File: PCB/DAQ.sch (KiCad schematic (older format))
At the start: 45 parts, among them IC1 MAX743CWE+, J1 Arduino_Mega_Header, J10 Conn_01x01, J11 Conn_01x01, J12 Conn_01x01, J2 Conn_01x07, J3 Conn_01x08, J4 Conn_01x08, J5 Conn_02x18_Counter_Clockwise, J6 Conn_01x10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

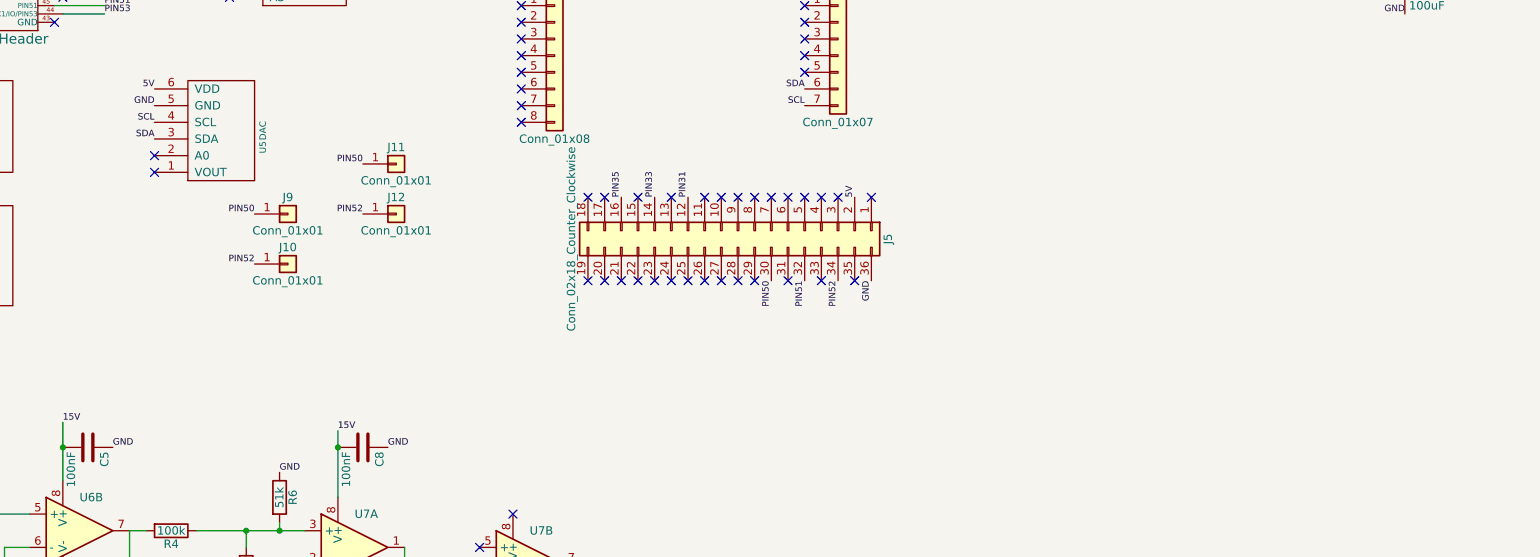
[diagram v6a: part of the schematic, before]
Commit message: Added analog part of DAC to PCB
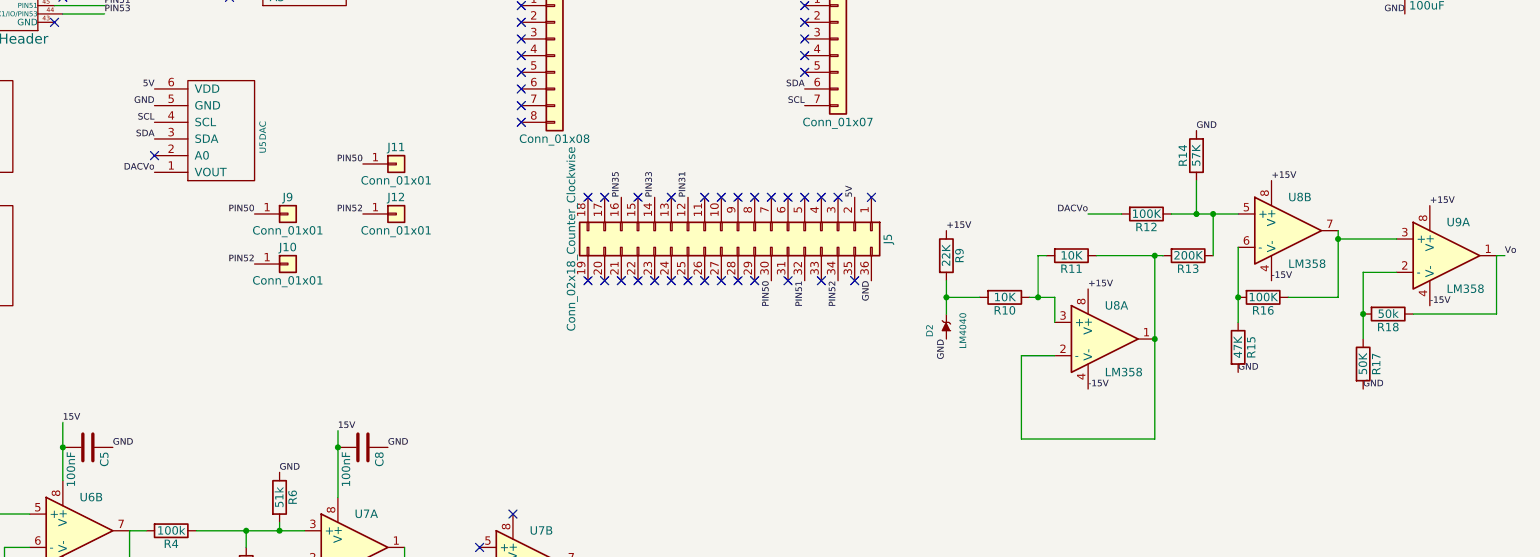
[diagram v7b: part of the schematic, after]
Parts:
- added D2: LM4040, TH-R:R-C-L-D, symbol LM4040
- added R10, R11: 10K, Resistors_THT:R_Axial_DIN0207_L6.3mm_D2.5mm_P7.62mm_Horizontal, symbol R
- added R12, R16: 100K, Resistors_THT:R_Axial_DIN0207_L6.3mm_D2.5mm_P7.62mm_Horizontal, symbol R
- added R13: 200K, Resistors_THT:R_Axial_DIN0207_L6.3mm_D2.5mm_P7.62mm_Horizontal, symbol R
- added R14: 57K, Resistors_THT:R_Axial_DIN0207_L6.3mm_D2.5mm_P7.62mm_Horizontal, symbol R
- added R15: 47K, Resistors_THT:R_Axial_DIN0207_L6.3mm_D2.5mm_P7.62mm_Horizontal, symbol R
- added R17: 50K, Resistors_THT:R_Axial_DIN0207_L6.3mm_D2.5mm_P7.62mm_Horizontal, symbol R
- added R18: 50k, Resistors_THT:R_Axial_DIN0207_L6.3mm_D2.5mm_P7.62mm_Horizontal, symbol R
- added R9: 22K, Resistors_THT:R_Axial_DIN0207_L6.3mm_D2.5mm_P7.62mm_Horizontal, symbol R
- added U8, U9: LM358, Housings_DIP:DIP-8_W7.62mm, symbol LM358
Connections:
- net +15V: now also R9.1, U8.8 (V+), U8.8 (V+), U9.8 (V+)
- net -15V: now also U8.4 (V-), U8.4 (V-), U9.4 (V-)
- net GND: now also D2.2 (A), R14.2, R15.2, R17.2
- net DACVo: now reaches U5.1 (VOUT)
- net DACVo: now also R12.2
- new net: R11.1, R13.2, U8.1, U8.2 (-)
- new net: R10.1, R11.2, U8.3 (+)
- new net: R17.1, R18.2, U9.2 (-)
- new net: R16.1, U8.7, U9.3 (+)
- new net: R12.1, R13.1, R14.1, U8.5 (+)
- new net: R15.1, R16.2, U8.6 (-)
- new net: D2.1 (K), R10.2, R9.2
- new net Vo: R18.1, U9.1
- no-connect marks 138 -> 137
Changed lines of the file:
@@
 NoConn ~ 3450 3500
 NoConn ~ 3000 4550
-NoConn ~ 3000 4650
 $Comp
 L Conn_01x07 J2
@@
 Text Label 3600 5200 2    39   ~ 0
 PIN52
+$Comp
+L LM358 U8
+U 1 1 5ACCFE80
+P 8700 5650
+F 0 "U8" H 8700 5850 50  0000 L CNN
+F 1 "LM358" H 8700 5450 50  0000 L CNN
+F 2 "Housings_DIP:DIP-8_W7.62mm" H 8700 5650 50  0001 C CNN
+F 3 "" H 8700 5650 50  0001 C CNN
+	1    8700 5650
+	1    0    0    -1
+$EndComp
+$Comp
+L LM358 U9
+U 1 1 5ACCFF07
+P 10750 5150
+F 0 "U9" H 10750 5350 50  0000 L CNN
+F 1 "LM358" H 10750 4950 50  0000 L CNN
+F 2 "Housings_DIP:DIP-8_W7.62mm" H 10750 5150 50  0001 C CNN
+F 3 "" H 10750 5150 50  0001 C CNN
+	1    10750 5150
+	1    0    0    -1
+$EndComp
+$Comp
+L LM358 U8
+U 2 1 5ACD0129
+P 9800 5000
+F 0 "U8" H 9800 5200 50  0000 L CNN
+F 1 "LM358" H 9800 4800 50  0000 L CNN
+F 2 "Housings_DIP:DIP-8_W7.62mm" H 9800 5000 50  0001 C CNN
+F 3 "" H 9800 5000 50  0001 C CNN
+	2    9800 5000
+	1    0    0    -1
+$EndComp
+$Comp
+L LM4040 D2
+U 1 1 5ACD0290
+P 7750 5600
+F 0 "D2" H 7750 5700 40  0000 C CNN
+F 1 "LM4040" H 7750 5500 40  0000 C CNN
+F 2 "TH-R:R-C-L-D" H 7750 5600 60  0001 C CNN
+F 3 "" H 7750 5600 60  0000 C CNN
+	1    7750 5600
+	0    -1   -1   0
+$EndComp
+$Comp
+L R R9
+U 1 1 5ACD033B
+P 7750 5150
+F 0 "R9" V 7830 5150 50  0000 C CNN
+F 1 "22K" V 7750 5150 50  0000 C CNN
+F 2 "Resistors_THT:R_Axial_DIN0207_L6.3mm_D2.5mm_P7.62mm_Horizontal" V 7680 5150 50  0001 C CNN
+F 3 "" H 7750 5150 50  0001 C CNN
+	1    7750 5150
+	1    0    0    -1
+$EndComp
+$Comp
+L R R10
+U 1 1 5ACD03DC
+P 8100 5400
+F 0 "R10" V 8180 5400 50  0000 C CNN
+F 1 "10K" V 8100 5400 50  0000 C CNN
+F 2 "Resistors_THT:R_Axial_DIN0207_L6.3mm_D2.5mm_P7.62mm_Horizontal" V 8030 5400 50  0001 C CNN
+F 3 "" H 8100 5400 50  0001 C CNN
+	1    8100 5400
+	0    1    1    0
+$EndComp
+$Comp
+L R R11
+U 1 1 5ACD04A7
+P 8500 5150
+F 0 "R11" V 8580 5150 50  0000 C CNN
+F 1 "10K" V 8500 5150 50  0000 C CNN
+F 2 "Resistors_THT:R_Axial_DIN0207_L6.3mm_D2.5mm_P7.62mm_Horizontal" V 8430 5150 50  0001 C CNN
+F 3 "" H 8500 5150 50  0001 C CNN
+	1    8500 5150
+	0    1    1    0
+$EndComp
+$Comp
+L R R12
+U 1 1 5ACD075C
+P 8950 4900
+F 0 "R12" V 9030 4900 50  0000 C CNN
+F 1 "100K" V 8950 4900 50  0000 C CNN
+F 2 "Resistors_THT:R_Axial_DIN0207_L6.3mm_D2.5mm_P7.62mm_Horizontal" V 8880 4900 50  0001 C CNN
+F 3 "" H 8950 4900 50  0001 C CNN
+	1    8950 4900
+	0    1    1    0
+$EndComp
+$Comp
+L R R14
+U 1 1 5ACD08D8
+P 9250 4550
+F 0 "R14" V 9330 4550 50  0000 C CNN
+F 1 "57K" V 9250 4550 50  0000 C CNN
+F 2 "Resistors_THT:R_Axial_DIN0207_L6.3mm_D2.5mm_P7.62mm_Horizontal" V 9180 4550 50  0001 C CNN
+F 3 "" H 9250 4550 50  0001 C CNN
+	1    9250 4550
+	-1   0    0    1
+$EndComp
+$Comp
+L R R15
+U 1 1 5ACD0977
+P 9500 5700
+F 0 "R15" V 9580 5700 50  0000 C CNN
+F 1 "47K" V 9500 5700 50  0000 C CNN
+F 2 "Resistors_THT:R_Axial_DIN0207_L6.3mm_D2.5mm_P7.62mm_Horizontal" V 9430 5700 50  0001 C CNN
+F 3 "" H 9500 5700 50  0001 C CNN
+	1    9500 5700
+	1    0    0    -1
+$EndComp
+$Comp
+L R R16
+U 1 1 5ACD0A0E
+P 9650 5400
+F 0 "R16" V 9730 5400 50  0000 C CNN
+F 1 "100K" V 9650 5400 50  0000 C CNN
+F 2 "Resistors_THT:R_Axial_DIN0207_L6.3mm_D2.5mm_P7.62mm_Horizontal" V 9580 5400 50  0001 C CNN
+F 3 "" H 9650 5400 50  0001 C CNN
+	1    9650 5400
+	0    1    1    0
+$EndComp
+$Comp
+L R R17
+U 1 1 5ACD0D00
+P 10250 5800
+F 0 "R17" V 10330 5800 50  0000 C CNN
+F 1 "50K" V 10250 5800 50  0000 C CNN
+F 2 "Resistors_THT:R_Axial_DIN0207_L6.3mm_D2.5mm_P7.62mm_Horizontal" V 10180 5800 50  0001 C CNN
+F 3 "" H 10250 5800 50  0001 C CNN
+	1    10250 5800
+	1    0    0    -1
+$EndComp
+$Comp
+L R R18
+U 1 1 5ACD0D06
+P 10400 5500
+F 0 "R18" V 10480 5500 50  0000 C CNN
+F 1 "50k" V 10400 5500 50  0000 C CNN
+F 2 "Resistors_THT:R_Axial_DIN0207_L6.3mm_D2.5mm_P7.62mm_Horizontal" V 10330 5500 50  0001 C CNN
+F 3 "" H 10400 5500 50  0001 C CNN
+	1    10400 5500
+	0    1    1    0
+$EndComp
+Text Label 7750 5650 3    39   ~ 0
+GND
+Wire Wire Line
+	7750 5500 7750 5300
+Wire Wire Line
+	7950 5400 7750 5400
+Connection ~ 7750 5400
+Text Label 7750 5000 0    39   ~ 0
++15V
+Wire Wire Line
+	8250 5400 8400 5400
+Wire Wire Line
+	8400 5400 8400 5550
+Wire Wire Line
+	8400 5750 8200 5750
+Wire Wire Line
+	8200 5750 8200 6250
+Wire Wire Line
+	8200 6250 9000 6250
+Wire Wire Line
+	9000 6250 9000 5150
+Wire Wire Line
+	8300 5400 8300 5150
+Wire Wire Line
+	8300 5150 8350 5150
+Connection ~ 8300 5400
+Wire Wire Line
+	8650 5150 9050 5150
+Connection ~ 9000 5650
+$Comp
+L R R13
+U 1 1 5ACD2C7F
+P 9200 5150
+F 0 "R13" V 9280 5150 50  0000 C CNN
+F 1 "200K" V 9200 5150 50  0000 C CNN
+F 2 "Resistors_THT:R_Axial_DIN0207_L6.3mm_D2.5mm_P7.62mm_Horizontal" V 9130 5150 50  0001 C CNN
+F 3 "" H 9200 5150 50  0001 C CNN
+	1    9200 5150
+	0    1    1    0
+$EndComp
+Connection ~ 9000 5150
+Wire Wire Line
+	9350 5150 9350 4900
+Wire Wire Line
+	9100 4900 9500 4900
+Connection ~ 9350 4900
+Wire Wire Line
+	9250 4700 9250 4900
+Connection ~ 9250 4900
+Wire Wire Line
+	8800 4900 8600 4900
+Text Label 9250 4400 0    39   ~ 0
+GND
+Text Label 8600 5350 0    39   ~ 0
++15V
+Text Label 8600 5950 0    39   ~ 0
+-15V
+Text Label 9700 4700 0    39   ~ 0
++15V
+Text Label 9700 5300 0    39   ~ 0
+-15V
+Text Label 10650 4850 0    39   ~ 0
++15V
+Text Label 10650 5450 0    39   ~ 0
+-15V
+Text Label 8600 4900 2    39   ~ 0
+DACVo
+Text Label 3000 4650 2    39   ~ 0
+DACVo
+Wire Wire Line
+	9500 5100 9500 5550
+Wire Wire Line
+	9800 5400 10100 5400
+Wire Wire Line
+	10100 5400 10100 5000
+Connection ~ 9500 5400
+Text Label 9500 5850 0    39   ~ 0
+GND
+Wire Wire Line
+	10450 5050 10100 5050
+Connection ~ 10100 5050
+Wire Wire Line
+	10450 5250 10250 5250
+Wire Wire Line
+	10250 5250 10250 5650
+Connection ~ 10250 5500
+Wire Wire Line
+	10550 5500 11050 5500
+Wire Wire Line
+	11050 5500 11050 5150
+Wire Wire Line
+	11050 5150 11100 5150
+Text Label 10250 5950 0    39   ~ 0
+GND
+Text Label 11100 5150 0    39   ~ 0
+Vo
 $EndSCHEMATC

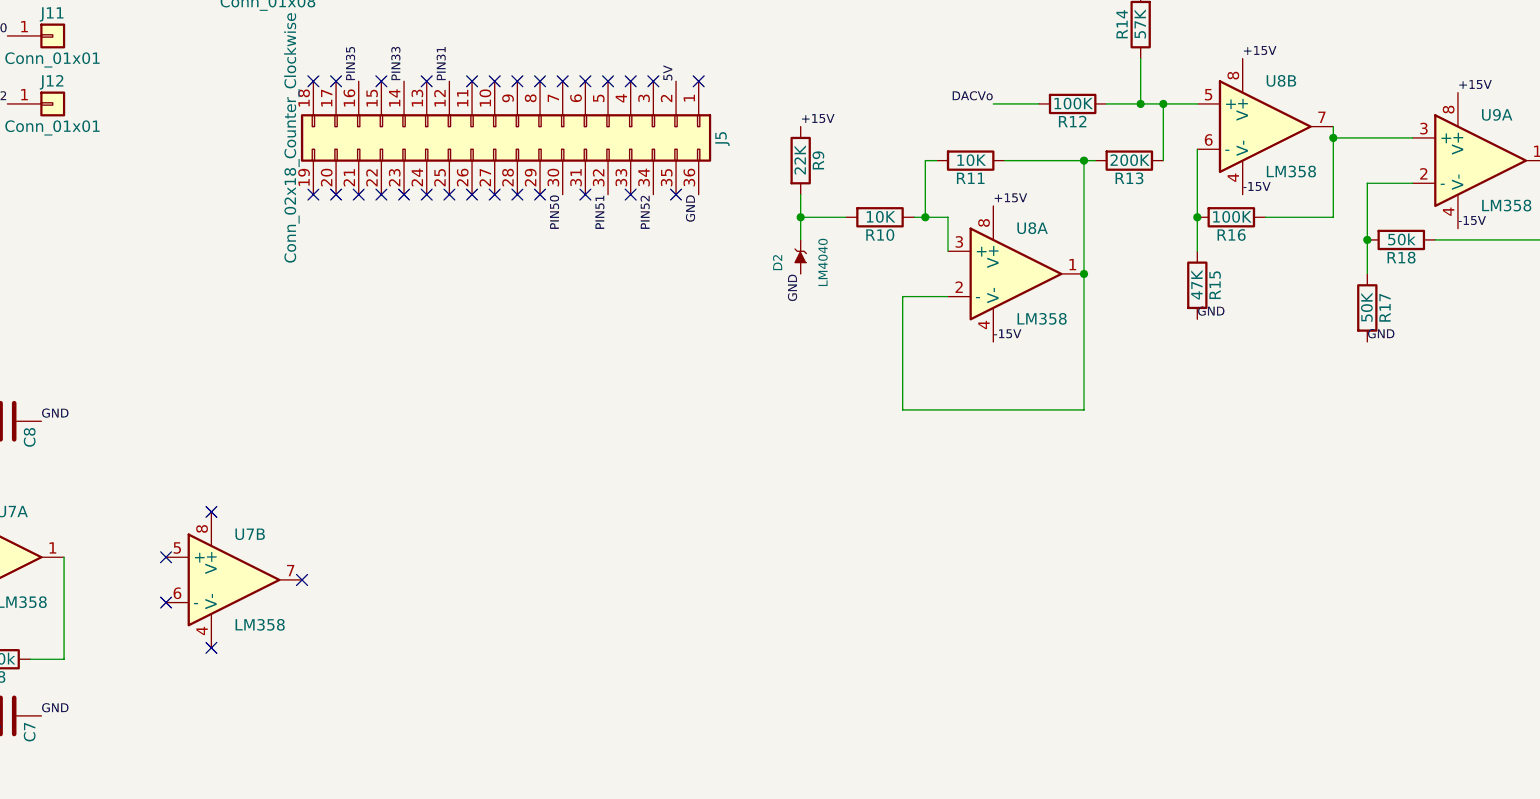
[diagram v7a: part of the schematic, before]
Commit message: Analog parts of the PCB upgraded
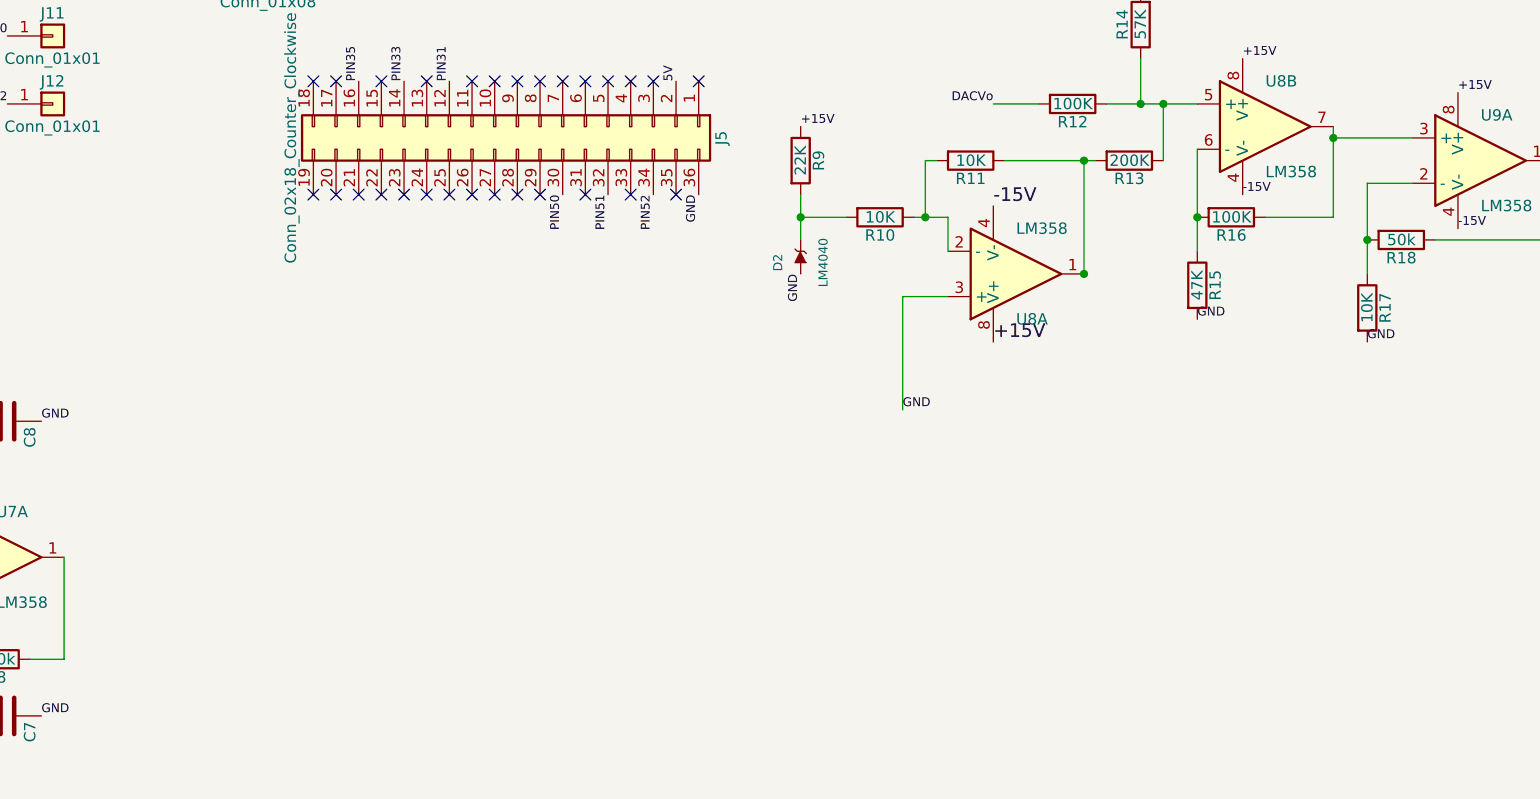
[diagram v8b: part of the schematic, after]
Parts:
- removed unit 2 of U7
- R17: value 50K -> 10K
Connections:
- net GND: now also U8.3 (+)
- net at R11.1, R13.2, U8.1: no longer U8.2 (-)
- net at R10.1, R11.2: now also U8.2 (-); no longer U8.3 (+)
- no-connect marks 137 -> 132
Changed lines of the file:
@@
 	0    1    1    0
 $EndComp
-$Comp
-L LM358 U7
-U 2 1 5AAC3CAA
-P 5250 7000
-F 0 "U7" H 5250 7200 50  0000 L CNN
-F 1 "LM358" H 5250 6800 50  0000 L CNN
-F 2 "Housings_DIP:DIP-8_W7.62mm" H 5250 7000 50  0001 C CNN
-F 3 "" H 5250 7000 50  0001 C CNN
-	2    5250 7000
-	1    0    0    -1
-$EndComp
-NoConn ~ 4950 6900
-NoConn ~ 4950 7100
-NoConn ~ 5150 7300
-NoConn ~ 5150 6700
-NoConn ~ 5550 7000
 Text Label 2450 6150 0    39   ~ 0
 15V
@@
 F 3 "" H 8700 5650 50  0001 C CNN
 	1    8700 5650
-	1    0    0    -1
+	1    0    0    1
 $EndComp
 $Comp
@@
 P 10250 5800
 F 0 "R17" V 10330 5800 50  0000 C CNN
-F 1 "50K" V 10250 5800 50  0000 C CNN
+F 1 "10K" V 10250 5800 50  0000 C CNN
 F 2 "Resistors_THT:R_Axial_DIN0207_L6.3mm_D2.5mm_P7.62mm_Horizontal" V 10180 5800 50  0001 C CNN
 F 3 "" H 10250 5800 50  0001 C CNN
@@
 	8200 5750 8200 6250
 Wire Wire Line
-	8200 6250 9000 6250
-Wire Wire Line
-	9000 6250 9000 5150
-Wire Wire Line
 	8300 5400 8300 5150
 Wire Wire Line
@@
 Text Label 9250 4400 0    39   ~ 0
 GND
-Text Label 8600 5350 0    39   ~ 0
-+15V
-Text Label 8600 5950 0    39   ~ 0
--15V
 Text Label 9700 4700 0    39   ~ 0
 +15V
@@
 Text Label 11100 5150 0    39   ~ 0
 Vo
+Text Label 8600 5350 0    60   ~ 0
+-15V
+Text Label 8600 5950 0    60   ~ 0
++15V
+Wire Wire Line
+	9000 5650 9000 5150
+Text Label 8200 6250 0    39   ~ 0
+GND
 $EndSCHEMATC
